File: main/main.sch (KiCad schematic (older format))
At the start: 16 parts, among them J1 USB_B_Micro, SW1 SW_SPST, SW2 SW_SPST, SW3 SW_SPST, SW4 SW_SPST, SW5 SW_SPST, SW6 SW_SPST, U1 LN6206P332MR-G

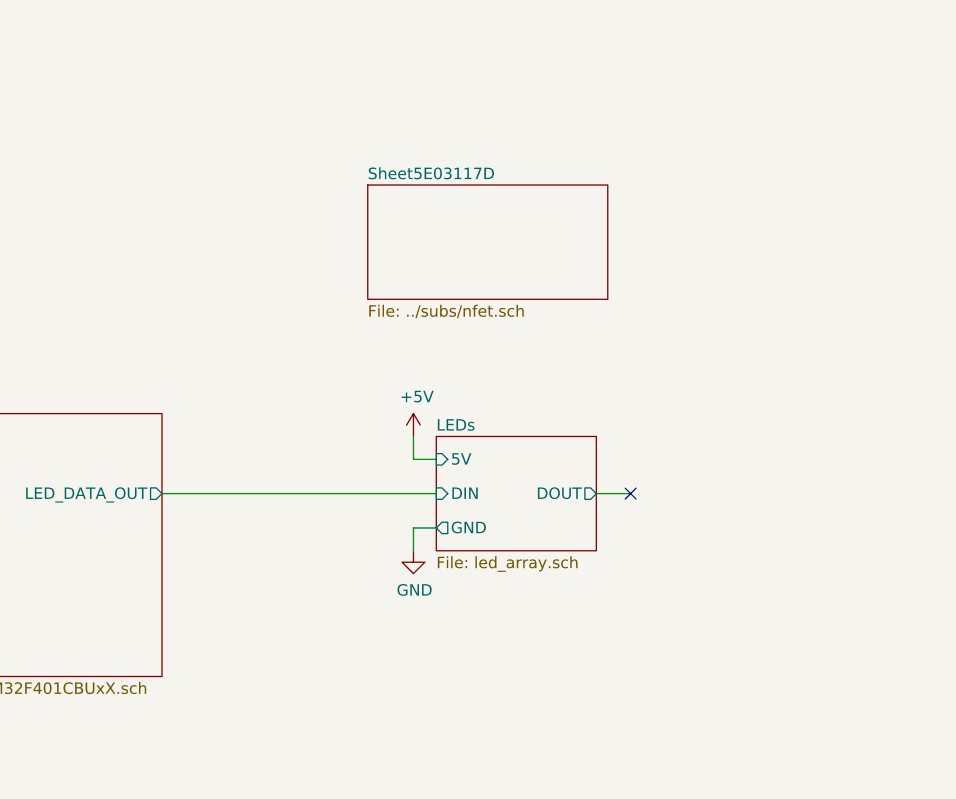
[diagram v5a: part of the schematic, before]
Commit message: mostly done?  reviewing now.  Also need to fix/update USB connector
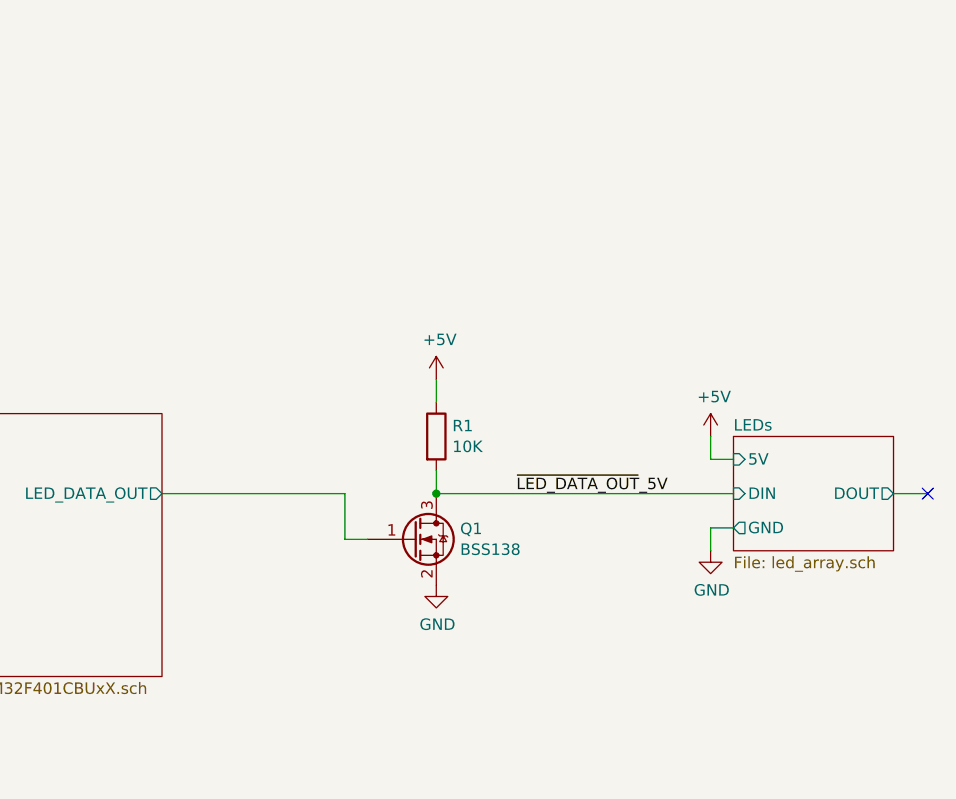
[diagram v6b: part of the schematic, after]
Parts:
- added Q1: BSS138, Package_TO_SOT_SMD:SOT-23, symbol Transistor_FET:BSS138
- added R1: 10K, Resistor_SMD:R_0402_1005Metric, symbol Device:R
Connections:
- net +5V: now also R1.1
- net GND: now also Q1.2 (S)
- new net mic/LED_DATA_OUT: Q1.1 (G)
- new net ~LED_DATA_OUT~_5V: Q1.3 (D), R1.2
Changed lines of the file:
@@
 $Descr A4 11693 8268
 encoding utf-8
-Sheet 1 5
+Sheet 1 4
 Title ""
 Date ""
@@
 $EndComp
 $Sheet
-S 6850 3250 700  500
+S 8150 3250 700  500
 U 5DEECD42
 F0 "LEDs" 50
 F1 "led_array.sch" 50
-F2 "5V" I L 6850 3350 50
-F3 "DIN" I L 6850 3500 50
-F4 "DOUT" O R 7550 3500 50
-F5 "GND" O L 6850 3650 50
+F2 "5V" I L 8150 3350 50
+F3 "DIN" I L 8150 3500 50
+F4 "DOUT" O R 8850 3500 50
+F5 "GND" O L 8150 3650 50
 $EndSheet
 $Comp
@@
 L power:+5V #PWR012
 U 1 1 5FA0C6C6
-P 6750 3250
-F 0 "#PWR012" H 6750 3100 50  0001 C CNN
-F 1 "+5V" H 6765 3423 50  0000 C CNN
-F 2 "" H 6750 3250 50  0001 C CNN
-F 3 "" H 6750 3250 50  0001 C CNN
-	1    6750 3250
-	1    0    0    -1
-$EndComp
-Wire Wire Line
-	6750 3250 6750 3350
-Wire Wire Line
-	6750 3350 6850 3350
+P 8050 3250
+F 0 "#PWR012" H 8050 3100 50  0001 C CNN
+F 1 "+5V" H 8065 3423 50  0000 C CNN
+F 2 "" H 8050 3250 50  0001 C CNN
+F 3 "" H 8050 3250 50  0001 C CNN
+	1    8050 3250
+	1    0    0    -1
+$EndComp
+Wire Wire Line
+	8050 3250 8050 3350
+Wire Wire Line
+	8050 3350 8150 3350
 $Comp
 L power:GND #PWR013
 U 1 1 5FA0FAFB
-P 6750 3750
-F 0 "#PWR013" H 6750 3500 50  0001 C CNN
-F 1 "GND" H 6755 3577 50  0000 C CNN
-F 2 "" H 6750 3750 50  0001 C CNN
-F 3 "" H 6750 3750 50  0001 C CNN
-	1    6750 3750
-	1    0    0    -1
-$EndComp
-Wire Wire Line
-	6750 3750 6750 3650
-Wire Wire Line
-	6750 3650 6850 3650
-Wire Wire Line
-	5650 3500 6850 3500
-NoConn ~ 7700 3500
-Wire Wire Line
-	7700 3500 7550 3500
+P 8050 3750
+F 0 "#PWR013" H 8050 3500 50  0001 C CNN
+F 1 "GND" H 8055 3577 50  0000 C CNN
+F 2 "" H 8050 3750 50  0001 C CNN
+F 3 "" H 8050 3750 50  0001 C CNN
+	1    8050 3750
+	1    0    0    -1
+$EndComp
+Wire Wire Line
+	8050 3750 8050 3650
+Wire Wire Line
+	8050 3650 8150 3650
+NoConn ~ 9000 3500
+Wire Wire Line
+	9000 3500 8850 3500
 Wire Wire Line
 	1050 5900 1050 5500
@@
 F 3 "" H 3850 3350 50  0001 C CNN
 	1    3850 3350
+	1    0    0    -1
+$EndComp
+Text Notes 2300 3900 0    50   ~ 0
+hour+
+Text Notes 2250 4700 0    50   ~ 0
+min+
+Text Notes 2250 5450 0    50   ~ 0
+mode
+Text Notes 2250 5900 0    50   ~ 0
+brightness
+Wire Wire Line
+	3850 4000 4400 4000
+Wire Wire Line
+	4400 3900 3850 3900
+Text Label 3850 4000 0    50   ~ 0
+SWITCH5
+Text Label 3850 3900 0    50   ~ 0
+SWITCH4
+Text Notes 2250 4300 0    50   ~ 0
+hour-
+Text Notes 2250 5050 0    50   ~ 0
+min-
+$Comp
+L Switch:SW_SPST SW2
+U 1 1 60E0254F
+P 1350 4300
+F 0 "SW2" H 1350 4535 50  0000 C CNN
+F 1 "SW_SPST" H 1350 4444 50  0000 C CNN
+F 2 "william_switch:KAN4562-0501C" H 1350 4300 50  0001 C CNN
+F 3 "~" H 1350 4300 50  0001 C CNN
+	1    1350 4300
+	1    0    0    -1
+$EndComp
+$Comp
+L Switch:SW_SPST SW3
+U 1 1 60E0418F
+P 1350 4700
+F 0 "SW3" H 1350 4935 50  0000 C CNN
+F 1 "SW_SPST" H 1350 4844 50  0000 C CNN
+F 2 "william_switch:KAN4562-0501C" H 1350 4700 50  0001 C CNN
+F 3 "~" H 1350 4700 50  0001 C CNN
+	1    1350 4700
+	1    0    0    -1
+$EndComp
+$Comp
+L Switch:SW_SPST SW4
+U 1 1 60E04199
+P 1350 5100
+F 0 "SW4" H 1350 5335 50  0000 C CNN
+F 1 "SW_SPST" H 1350 5244 50  0000 C CNN
+F 2 "william_switch:KAN4562-0501C" H 1350 5100 50  0001 C CNN
+F 3 "~" H 1350 5100 50  0001 C CNN
+	1    1350 5100
+	1    0    0    -1
+$EndComp
+$Comp
+L Switch:SW_SPST SW5
+U 1 1 60E05E72
+P 1350 5500
+F 0 "SW5" H 1350 5735 50  0000 C CNN
+F 1 "SW_SPST" H 1350 5644 50  0000 C CNN
+F 2 "william_switch:KAN4562-0501C" H 1350 5500 50  0001 C CNN
+F 3 "~" H 1350 5500 50  0001 C CNN
+	1    1350 5500
+	1    0    0    -1
+$EndComp
+$Comp
+L Switch:SW_SPST SW6
+U 1 1 60E05E7C
+P 1350 5900
+F 0 "SW6" H 1350 6135 50  0000 C CNN
+F 1 "SW_SPST" H 1350 6044 50  0000 C CNN
+F 2 "william_switch:KAN4562-0501C" H 1350 5900 50  0001 C CNN
+F 3 "~" H 1350 5900 50  0001 C CNN
+	1    1350 5900
+	1    0    0    -1
+$EndComp
+Wire Wire Line
+	2800 1100 3350 1100
+Wire Wire Line
+	2800 1400 3650 1400
+Text Notes 4150 1600 0    50   ~ 0
+LCSC pn:\nC141407
+$Comp
+L william_dc_ldo:LN6206P332MR-G U1
+U 1 1 5DF1CFB8
+P 3650 1150
+F 0 "U1" H 3650 1442 50  0000 C CNN
+F 1 "LN6206P332MR-G" H 3650 1351 50  0000 C CNN
+F 2 "Package_TO_SOT_SMD:SOT-23" H 3800 1500 50  0001 C CNN
+F 3 "https://datasheet.lcsc.com/szlcsc/1810311908_NATLINEAR-LN6206P332MR-G_C141407.pdf" H 3800 1500 50  0001 C CNN
+	1    3650 1150
+	1    0    0    -1
+$EndComp
+Text Notes 1550 2450 0    50   ~ 0
+RTC cell
+$Comp
+L william_connectors:CR2032-BS-6-1 BT1
+U 1 1 5DF2AF87
+P 1200 2750
+F 0 "BT1" H 1318 2846 50  0000 L CNN
+F 1 "CR2032-BS-6-1" H 1318 2755 50  0000 L CNN
+F 2 "william_batteries:CR2032-BS-6-1" V 1200 2810 50  0001 C CNN
+F 3 "https://datasheet.lcsc.com/szlcsc/1811061923_Q-J-CR2032-BS-6-1_C70377.pdf" V 1200 2810 50  0001 C CNN
+	1    1200 2750
+	1    0    0    -1
+$EndComp
+$Comp
+L Transistor_FET:BSS138 Q1
+U 1 1 5E038DFC
+P 6750 3700
+F 0 "Q1" H 6954 3746 50  0000 L CNN
+F 1 "BSS138" H 6954 3655 50  0000 L CNN
+F 2 "Package_TO_SOT_SMD:SOT-23" H 6950 3625 50  0001 L CIN
+F 3 "https://www.fairchildsemi.com/datasheets/BS/BSS138.pdf" H 6750 3700 50  0001 L CNN
+	1    6750 3700
 	1    0    0    -1
 $EndComp
@@
 F11 "SWITCH5" I L 4400 4000 50
 $EndSheet
-Text Notes 2300 3900 0    50   ~ 0
-hour+
-Text Notes 2250 4700 0    50   ~ 0
-min+
-Text Notes 2250 5450 0    50   ~ 0
-mode
-Text Notes 2250 5900 0    50   ~ 0
-brightness
-Wire Wire Line
-	3850 4000 4400 4000
-Wire Wire Line
-	4400 3900 3850 3900
-Text Label 3850 4000 0    50   ~ 0
-SWITCH5
-Text Label 3850 3900 0    50   ~ 0
-SWITCH4
-Text Notes 2250 4300 0    50   ~ 0
-hour-
-Text Notes 2250 5050 0    50   ~ 0
-min-
-$Comp
-L Switch:SW_SPST SW2
-U 1 1 60E0254F
-P 1350 4300
-F 0 "SW2" H 1350 4535 50  0000 C CNN
-F 1 "SW_SPST" H 1350 4444 50  0000 C CNN
-F 2 "william_switch:KAN4562-0501C" H 1350 4300 50  0001 C CNN
-F 3 "~" H 1350 4300 50  0001 C CNN
-	1    1350 4300
-	1    0    0    -1
-$EndComp
-$Comp
-L Switch:SW_SPST SW3
-U 1 1 60E0418F
-P 1350 4700
-F 0 "SW3" H 1350 4935 50  0000 C CNN
-F 1 "SW_SPST" H 1350 4844 50  0000 C CNN
-F 2 "william_switch:KAN4562-0501C" H 1350 4700 50  0001 C CNN
-F 3 "~" H 1350 4700 50  0001 C CNN
-	1    1350 4700
-	1    0    0    -1
-$EndComp
-$Comp
-L Switch:SW_SPST SW4
-U 1 1 60E04199
-P 1350 5100
-F 0 "SW4" H 1350 5335 50  0000 C CNN
-F 1 "SW_SPST" H 1350 5244 50  0000 C CNN
-F 2 "william_switch:KAN4562-0501C" H 1350 5100 50  0001 C CNN
-F 3 "~" H 1350 5100 50  0001 C CNN
-	1    1350 5100
-	1    0    0    -1
-$EndComp
-$Comp
-L Switch:SW_SPST SW5
-U 1 1 60E05E72
-P 1350 5500
-F 0 "SW5" H 1350 5735 50  0000 C CNN
-F 1 "SW_SPST" H 1350 5644 50  0000 C CNN
-F 2 "william_switch:KAN4562-0501C" H 1350 5500 50  0001 C CNN
-F 3 "~" H 1350 5500 50  0001 C CNN
-	1    1350 5500
-	1    0    0    -1
-$EndComp
-$Comp
-L Switch:SW_SPST SW6
-U 1 1 60E05E7C
-P 1350 5900
-F 0 "SW6" H 1350 6135 50  0000 C CNN
-F 1 "SW_SPST" H 1350 6044 50  0000 C CNN
-F 2 "william_switch:KAN4562-0501C" H 1350 5900 50  0001 C CNN
-F 3 "~" H 1350 5900 50  0001 C CNN
-	1    1350 5900
-	1    0    0    -1
-$EndComp
-Wire Wire Line
-	2800 1100 3350 1100
-Wire Wire Line
-	2800 1400 3650 1400
-Text Notes 4150 1600 0    50   ~ 0
-LCSC pn:\nC141407
-$Comp
-L william_dc_ldo:LN6206P332MR-G U1
-U 1 1 5DF1CFB8
-P 3650 1150
-F 0 "U1" H 3650 1442 50  0000 C CNN
-F 1 "LN6206P332MR-G" H 3650 1351 50  0000 C CNN
-F 2 "Package_TO_SOT_SMD:SOT-23" H 3800 1500 50  0001 C CNN
-F 3 "https://datasheet.lcsc.com/szlcsc/1810311908_NATLINEAR-LN6206P332MR-G_C141407.pdf" H 3800 1500 50  0001 C CNN
-	1    3650 1150
-	1    0    0    -1
-$EndComp
-Text Notes 1550 2450 0    50   ~ 0
-RTC cell
-$Comp
-L william_connectors:CR2032-BS-6-1 BT1
-U 1 1 5DF2AF87
-P 1200 2750
-F 0 "BT1" H 1318 2846 50  0000 L CNN
-F 1 "CR2032-BS-6-1" H 1318 2755 50  0000 L CNN
-F 2 "william_batteries:CR2032-BS-6-1" V 1200 2810 50  0001 C CNN
-F 3 "https://datasheet.lcsc.com/szlcsc/1811061923_Q-J-CR2032-BS-6-1_C70377.pdf" V 1200 2810 50  0001 C CNN
-	1    1200 2750
-	1    0    0    -1
-$EndComp
-$Sheet
-S 6550 2150 1050 500
-U 5E03117E
-F0 "Sheet5E03117D" 50
-F1 "../subs/nfet.sch" 50
-$EndSheet
+Wire Wire Line
+	5650 3500 6450 3500
+Wire Wire Line
+	6450 3500 6450 3700
+Wire Wire Line
+	6450 3700 6550 3700
+$Comp
+L power:GND #PWR0101
+U 1 1 5E040116
+P 6850 3900
+F 0 "#PWR0101" H 6850 3650 50  0001 C CNN
+F 1 "GND" H 6855 3727 50  0000 C CNN
+F 2 "" H 6850 3900 50  0001 C CNN
+F 3 "" H 6850 3900 50  0001 C CNN
+	1    6850 3900
+	1    0    0    -1
+$EndComp
+$Comp
+L Device:R R1
+U 1 1 5E1574DE
+P 6850 3250
+F 0 "R1" H 6920 3296 50  0000 L CNN
+F 1 "10K" H 6920 3205 50  0000 L CNN
+F 2 "Resistor_SMD:R_0402_1005Metric" V 6780 3250 50  0001 C CNN
+F 3 "~" H 6850 3250 50  0001 C CNN
+	1    6850 3250
+	1    0    0    -1
+$EndComp
+$Comp
+L power:+5V #PWR0102
+U 1 1 5E157D92
+P 6850 3000
+F 0 "#PWR0102" H 6850 2850 50  0001 C CNN
+F 1 "+5V" H 6865 3173 50  0000 C CNN
+F 2 "" H 6850 3000 50  0001 C CNN
+F 3 "" H 6850 3000 50  0001 C CNN
+	1    6850 3000
+	1    0    0    -1
+$EndComp
+Wire Wire Line
+	6850 3000 6850 3100
+Wire Wire Line
+	6850 3400 6850 3500
+Wire Wire Line
+	6850 3500 8150 3500
+Connection ~ 6850 3500
+Text Label 7200 3500 0    50   ~ 0
+~LED_DATA_OUT~_5V
 $EndSCHEMATC

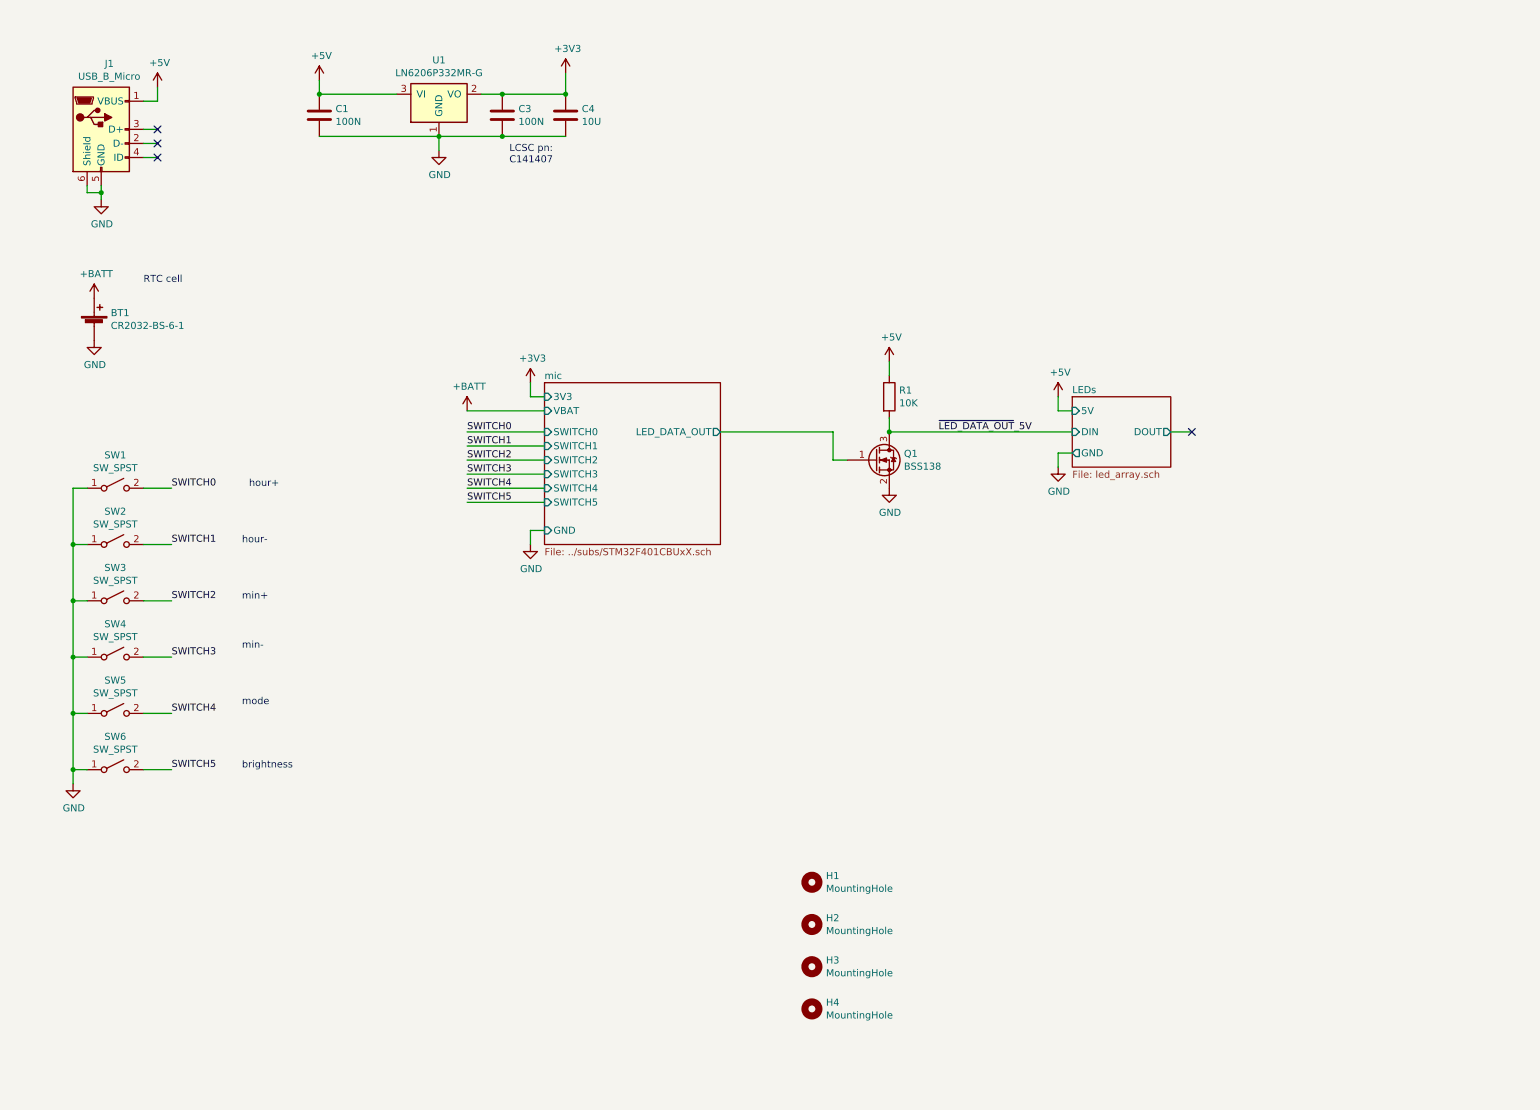
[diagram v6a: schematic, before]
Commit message: caps done, added FET for 5V logic to WS2813, reduced trace/space
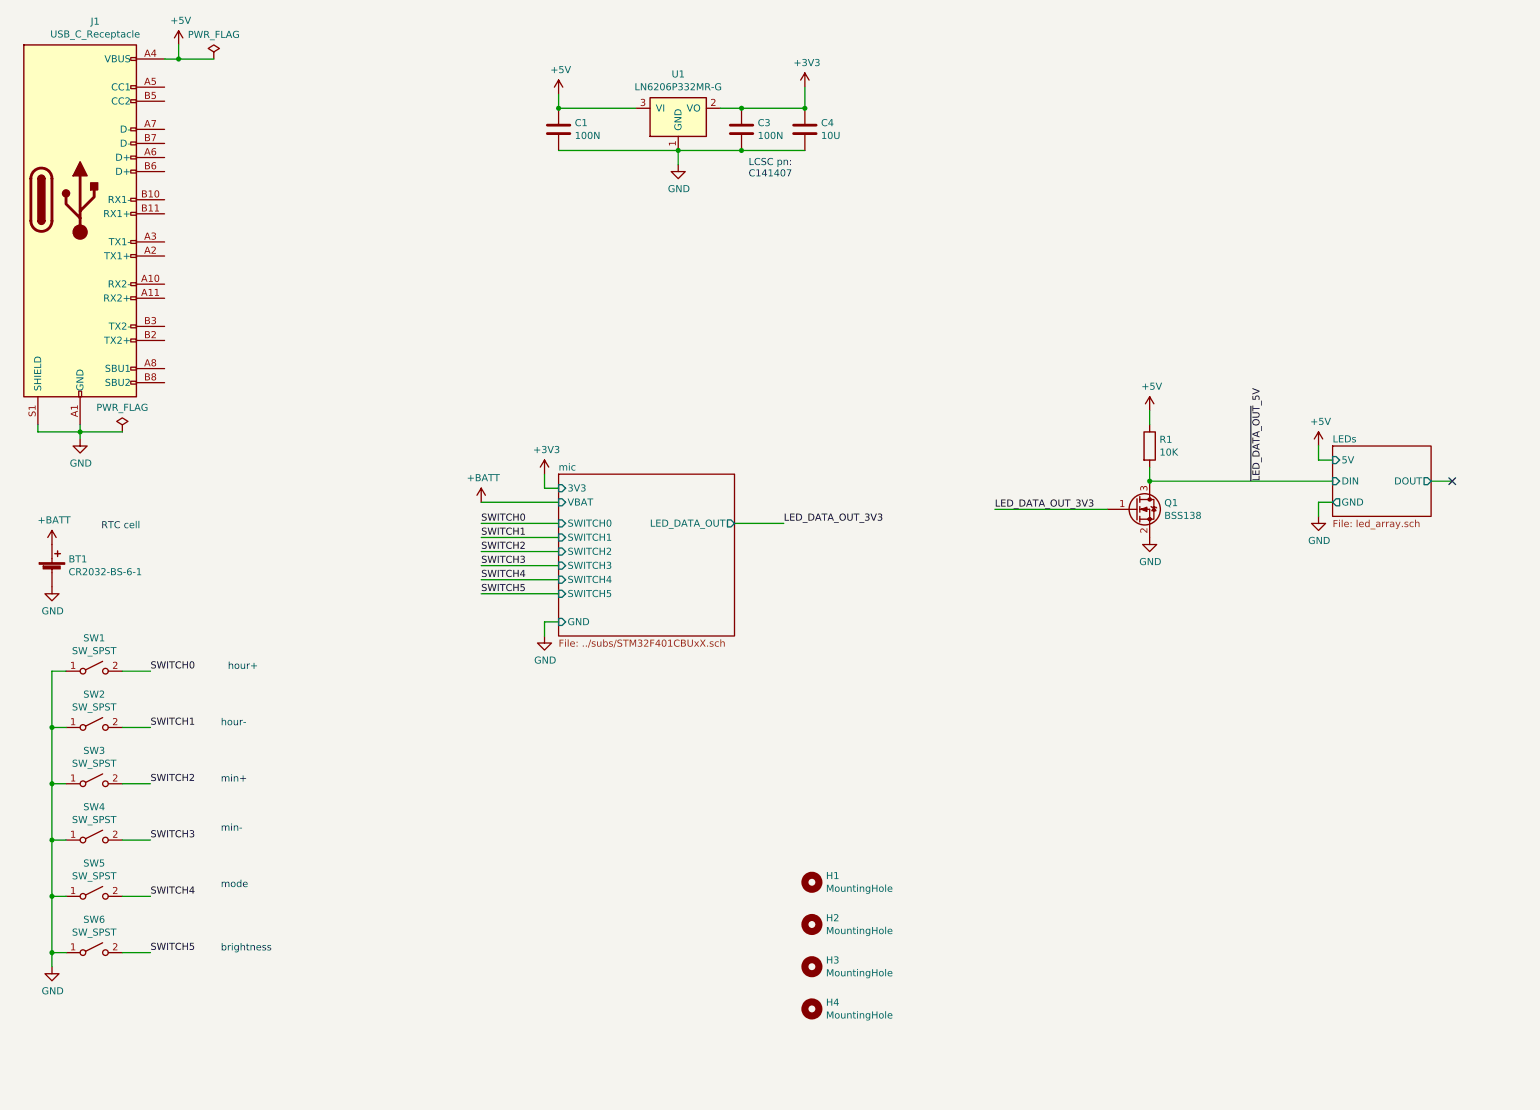
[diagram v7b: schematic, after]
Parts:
- removed J1: USB_B_Micro, Connector_USB:USB_Micro-B_GCT_USB3076-30-A, symbol Connector:USB_B_Micro
- added J1: USB_C_Receptacle, william_usb:C168688, symbol Connector:USB_C_Receptacle
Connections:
- net +5V: now also J1.A4 (VBUS), J1.A9 (VBUS), J1.B4 (VBUS), J1.B9 (VBUS)
- net GND: now also J1.A1 (GND), J1.A12 (GND), J1.B1 (GND), J1.B12 (GND), J1.S1 (SHIELD)
- net mic/LED_DATA_OUT renamed LED_DATA_OUT_3V3
- no-connect marks 4 -> 1
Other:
- moved on the sheet: BT1, C1, C3, C4, Q1, R1, SW1, SW2, SW3, SW4, SW5, SW6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
